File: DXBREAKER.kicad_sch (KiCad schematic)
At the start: 15 parts, among them J1 PINS_LEFT, J2 PINS_RIGHT, SW1 RESET, SW2 FLASH, U1 ESP-12F, U2 AMS1117-3.3

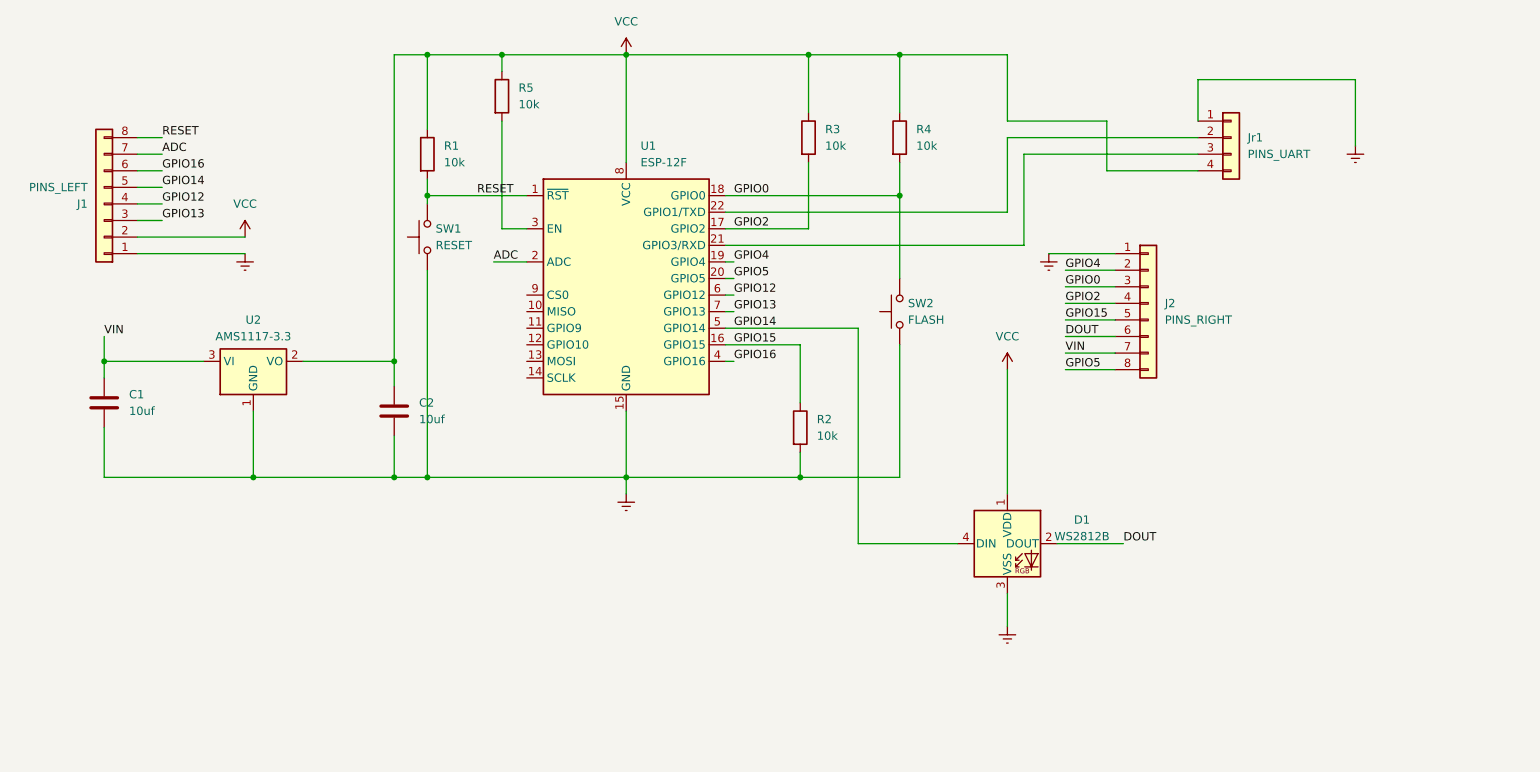
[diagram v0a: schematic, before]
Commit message: Update schematics for Rev.2.0
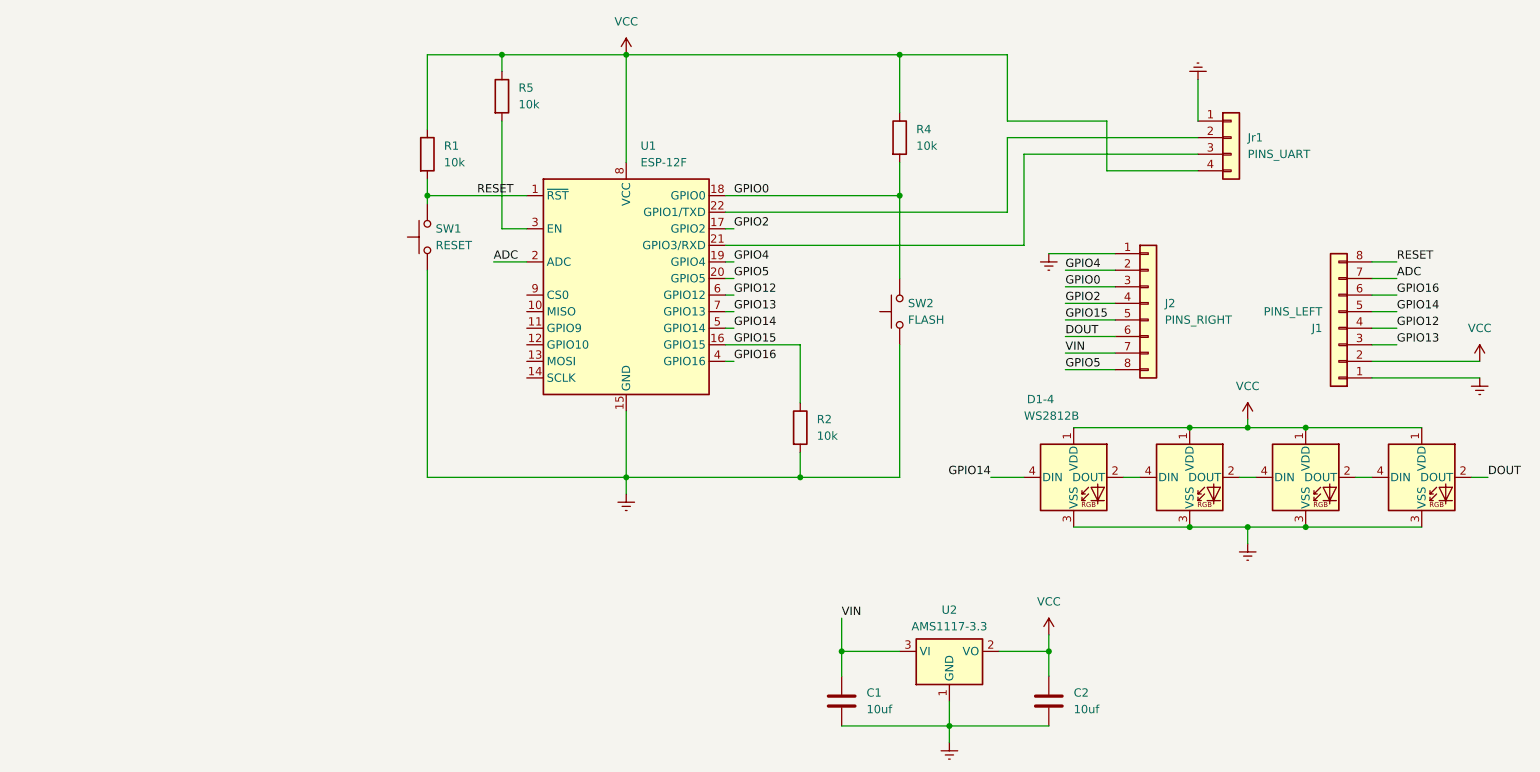
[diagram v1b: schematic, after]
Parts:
- removed R3: 10k, Resistor_SMD:R_0805_2012Metric_Pad1.20x1.40mm_HandSolder, symbol Device:R
- added D2, D3, D4: WS2812B, LED_SMD:LED_WS2812B_PLCC4_5.0x5.0mm_P3.2mm, symbol LED:WS2812B
- renumbered D1 to D1-4
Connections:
- net DOUT: now also D4.2 (DOUT); no longer D1-4.2 (DOUT)
- net Earth: now also D2.3 (VSS), D3.3 (VSS), D4.3 (VSS)
- net VCC: now also D2.1 (VDD), D3.1 (VDD), D4.1 (VDD)
- new net: D1-4.2 (DOUT), D2.4 (DIN)
- new net: D3.2 (DOUT), D4.4 (DIN)
- new net: D2.2 (DOUT), D3.4 (DIN)
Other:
- title: (none) -> DX8266 "BREAKER"
- moved on the sheet: C1, C2, D1-4, J1, U2
